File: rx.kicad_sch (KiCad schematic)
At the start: 49 parts, among them J5 SWH, J7 SMA, J9 SWH, T1 RF_BALUN, T1 RXIF_BALUN, U14 MAX2120, U16 DPDT

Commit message: Add footprints
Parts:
- C86, C89: footprint (none) -> Capacitor_SMD:C_0201_0603Metric
- FL2: footprint (none) -> mainboard:Filter_Pulse_LPF1005LL50R2400A_1.5x0.5mm
- J5, J9: footprint (none) -> mainboard:Murata_SWH_MM8930-26xx
- J7: footprint (none) -> mainboard:Linx_SMA_CONSMA003.062
- L6, L7: footprint (none) -> Inductor_SMD:L_0201_0603Metric
- R58, R59: footprint (none) -> Resistor_SMD:R_0201_0603Metric
- T1: footprint (none) -> RF_Converter:Balun_Johanson_0896BM15A0001
- T1: footprint (none) -> RF_Converter:Anaren_0805_2012Metric-6
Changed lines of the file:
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@@
       (effects (font (size 1.27 1.27)) (justify left))
     )
-    (property "Footprint" "" (at 110.1852 124.46 0)
+    (property "Footprint" "Capacitor_SMD:C_0201_0603Metric" (at 110.1852 124.46 0)
       (effects (font (size 1.27 1.27)) hide)
     )
@@
       (effects (font (size 1.27 1.27)))
     )
-    (property "Footprint" "" (at 124.1552 96.52 0)
+    (property "Footprint" "Capacitor_SMD:C_0201_0603Metric" (at 124.1552 96.52 0)
       (effects (font (size 1.27 1.27)) hide)
     )
@@
       (effects (font (size 1.27 1.27)))
     )
-    (property "Footprint" "" (at 179.07 44.45 0)
+    (property "Footprint" "mainboard:Filter_Pulse_LPF1005LL50R2400A_1.5x0.5mm" (at 179.07 44.45 0)
       (effects (font (size 1.27 1.27)) hide)
     )
@@
       (effects (font (size 1.27 1.27)))
     )
-    (property "Footprint" "" (at 121.412 91.44 90)
+    (property "Footprint" "Resistor_SMD:R_0201_0603Metric" (at 121.412 91.44 90)
       (effects (font (size 1.27 1.27)) hide)
     )
@@
       (effects (font (size 1.27 1.27)))
     )
-    (property "Footprint" "" (at 162.56 57.15 0)
+    (property "Footprint" "mainboard:Murata_SWH_MM8930-26xx" (at 162.56 57.15 0)
       (effects (font (size 1.27 1.27)) hide)
     )
@@
       (effects (font (size 1.27 1.27)))
     )
-    (property "Footprint" "" (at 232.41 101.6 0)
+    (property "Footprint" "RF_Converter:Balun_Johanson_0896BM15A0001" (at 232.41 101.6 0)
       (effects (font (size 1.27 1.27)) hide)
     )
@@
       (effects (font (size 1.27 1.27)))
     )
-    (property "Footprint" "" (at 231.14 67.31 0)
+    (property "Footprint" "mainboard:Murata_SWH_MM8930-26xx" (at 231.14 67.31 0)
       (effects (font (size 1.27 1.27)) hide)
     )
@@
       (effects (font (size 1.27 1.27)) (justify left))
     )
-    (property "Footprint" "" (at 185.42 90.17 0)
+    (property "Footprint" "Inductor_SMD:L_0201_0603Metric" (at 185.42 90.17 0)
       (effects (font (size 1.27 1.27)) hide)
     )
@@
       (effects (font (size 1.27 1.27)) (justify left))
     )
-    (property "Footprint" "" (at 224.79 92.71 0)
+    (property "Footprint" "Inductor_SMD:L_0201_0603Metric" (at 224.79 92.71 0)
       (effects (font (size 1.27 1.27)) hide)
     )
@@
       (effects (font (size 1.27 1.27)))
     )
-    (property "Footprint" "" (at 128.27 88.138 90)
+    (property "Footprint" "Resistor_SMD:R_0201_0603Metric" (at 128.27 88.138 90)
       (effects (font (size 1.27 1.27)) hide)
     )
@@
       (effects (font (size 1.27 1.27)))
     )
-    (property "Footprint" "" (at 176.53 99.06 0)
+    (property "Footprint" "RF_Converter:Anaren_0805_2012Metric-6" (at 176.53 99.06 0)
       (effects (font (size 1.27 1.27)) hide)
     )
@@
       (effects (font (size 1.27 1.27)) (justify left))
     )
-    (property "Footprint" "" (at 257.81 57.15 0)
-      (effects (font (size 1.27 1.27)) hide)
-    )
+    (property "Footprint" "mainboard:Linx_SMA_CONSMA003.062" (at 257.81 57.15 0)
+      (effects (font (size 1.27 1.27)) hide)
+    )

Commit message: Add more footprints
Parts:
- U16: footprint eval:QFN-12-1EP_2x2mm_P0.5mm_EP1x1mm -> mainboard:QFN-12-1EP_2x2mm_P0.5mm_EP1x1mm
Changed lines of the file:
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@@
       (effects (font (size 1.27 1.27)) (justify right))
     )
-    (property "Footprint" "eval:QFN-12-1EP_2x2mm_P0.5mm_EP1x1mm" (at 200.66 57.15 0)
+    (property "Footprint" "mainboard:QFN-12-1EP_2x2mm_P0.5mm_EP1x1mm" (at 200.66 57.15 0)
       (effects (font (size 1.27 1.27)) hide)
     )

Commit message: layout wip
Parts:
- added C159 (x2): 1uF, Capacitor_SMD:C_0201_0603Metric, symbol Device:C
- added J13: RFShield_Frame, RF_Shielding:Laird_Technologies_BMI-S-203-F_26.21x26.21mm, symbol Device:RFShield_OnePiece
- C159, C36: footprint Capacitor_SMD:C_0402_1005Metric -> Capacitor_SMD:C_0201_0603Metric; Manufacturer Samsung -> Murata; Part Number CL05A105KP5NNNC -> GRM033R61A105ME44D; Substitution any equivalent -> GRM033R61A105ME44*, GRM033R61C105ME15*, Samsung CL03A105MO3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
- C5: footprint Capacitor_SMD:C_0402_1005Metric -> Capacitor_SMD:C_0201_0603Metric; Manufacturer Samsung -> Murata; Part Number CL05B102KB5NNNC -> GRM033R71E102KA01D; Substitution any equivalent -> GRM033R71E102KA01*
- U16: footprint mainboard:QFN-12-1EP_2x2mm_P0.5mm_EP1x1mm -> mainboard:QFN-12-1EP_2x2mm_P0.5mm_EP1x1mm_ThermalVias
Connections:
- net 3V3RX: now also C159.1, C159.1
- net GND: now also C159.2, C159.2, J13.1 (Shield)
- net RX Mixer/MIX_IN+: now also L6.2, T1.4; no longer L6.1, T1.3
- net RX Mixer/MIX_IN-: now also L6.1, T1.3; no longer L6.2, T1.4

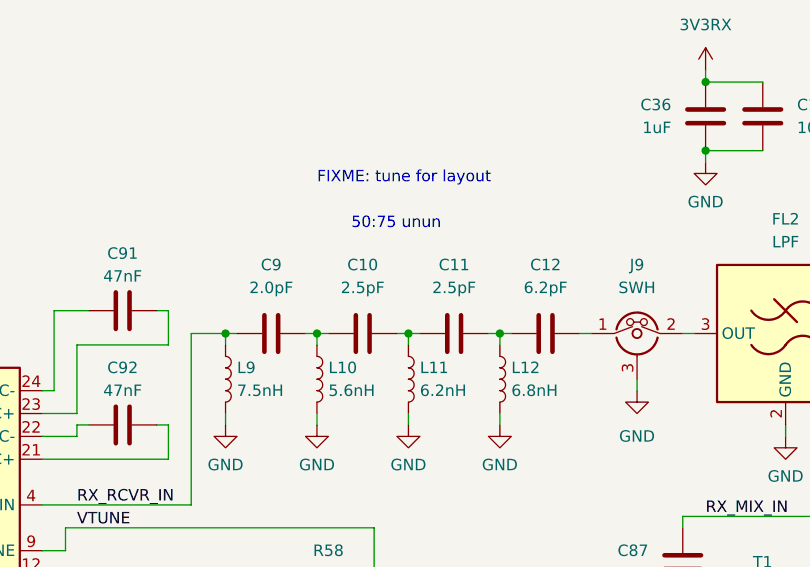
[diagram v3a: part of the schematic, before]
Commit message: tune unun for layout
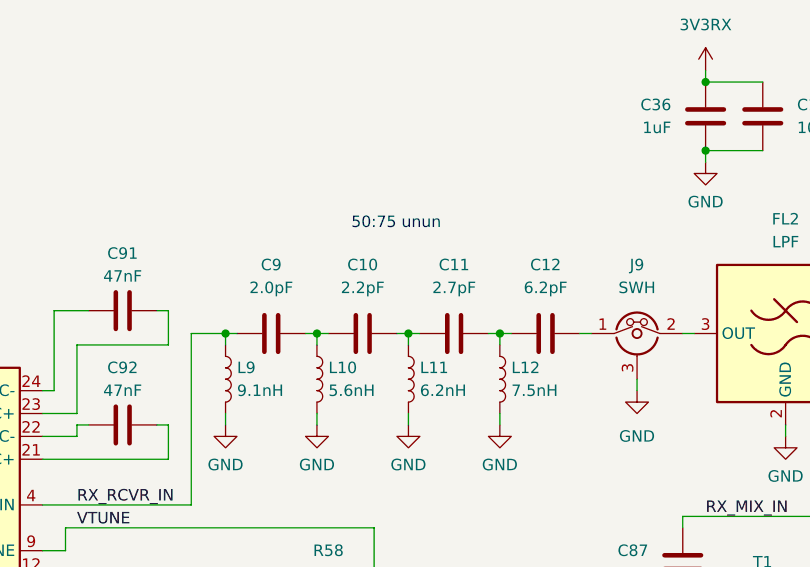
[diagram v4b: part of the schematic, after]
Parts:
- C10: value 2.5pF -> 2.2pF; Part Number GRM0335C1H2R5BA01D -> GRM0335C1H2R2BA01D; Substitution GRM0335C1H2R5BA01* -> GRM0335C1H2R2BA01*
- C11: value 2.5pF -> 2.7pF; Part Number GRM0335C1H2R5BA01D -> GRM0335C1H2R7BA01D; Substitution GRM0335C1H2R5BA01* -> GRM0335C1H2R7BA01*
- L12: value 6.8nH -> 7.5nH; Part Number LQP03HQ6N8H02D -> LQP03HQ7N5H02D
- L9: value 7.5nH -> 9.1nH; Part Number LQP03HQ7N5H02D -> LQP03HQ9N1H02D
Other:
- note removed: "FIXME: tune for layout"
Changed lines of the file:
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@@
-    (effects (font (size 1.27 1.27)) (justify left bottom))
-  )
-  (text "FIXME: tune for layout" (at 127 40.64 0)
     (effects (font (size 1.27 1.27)) (justify left bottom))
   )
@@
       (effects (font (size 1.27 1.27)))
     )
-    (property "Value" "2.5pF" (at 132.08 52.07 90)
+    (property "Value" "2.2pF" (at 132.08 52.07 90)
       (effects (font (size 1.27 1.27)))
     )
@@
       (effects (font (size 1.27 1.27)) hide)
     )
-    (property "Description" "CAP CER 2.5PF 50V C0G/NP0 0201" (at 132.08 57.15 0)
+    (property "Description" "CAP CER 2.2PF 50V C0G/NP0 0201" (at 132.08 57.15 0)
       (effects (font (size 1.27 1.27)) hide)
     )
@@
       (effects (font (size 1.27 1.27)) hide)
     )
-    (property "Part Number" "GRM0335C1H2R5BA01D" (at 132.08 57.15 0)
-      (effects (font (size 1.27 1.27)) hide)
-    )
-    (property "Substitution" "GRM0335C1H2R5BA01*" (at 132.08 57.15 0)
+    (property "Part Number" "GRM0335C1H2R2BA01D" (at 132.08 57.15 0)
+      (effects (font (size 1.27 1.27)) hide)
+    )
+    (property "Substitution" "GRM0335C1H2R2BA01*" (at 132.08 57.15 0)
       (effects (font (size 1.27 1.27)) hide)
     )
@@
       (effects (font (size 1.27 1.27)) (justify left))
     )
-    (property "Value" "7.5nH" (at 118.11 63.5 0)
+    (property "Value" "9.1nH" (at 118.11 63.5 0)
       (effects (font (size 1.27 1.27)) (justify left))
     )
@@
       (effects (font (size 1.27 1.27)) hide)
     )
-    (property "Description" "FIXED IND 7.5NH 400MA 300MOHM SM" (at 116.84 62.23 0)
+    (property "Description" "FIXED IND 9.1NH 300MA 400MOHM SM" (at 116.84 62.23 0)
       (effects (font (size 1.27 1.27)) hide)
     )
@@
       (effects (font (size 1.27 1.27)) hide)
     )
-    (property "Part Number" "LQP03HQ7N5H02D" (at 116.84 62.23 0)
+    (property "Part Number" "LQP03HQ9N1H02D" (at 116.84 62.23 0)
       (effects (font (size 1.27 1.27)) hide)
     )
@@
       (effects (font (size 1.27 1.27)) (justify left))
     )
-    (property "Value" "6.8nH" (at 148.59 63.5 0)
+    (property "Value" "7.5nH" (at 148.59 63.5 0)
       (effects (font (size 1.27 1.27)) (justify left))
     )
@@
       (effects (font (size 1.27 1.27)) hide)
     )
-    (property "Description" "FIXED IND 6.8NH 400MA 300MOHM SM" (at 147.32 62.23 0)
+    (property "Description" "FIXED IND 7.5NH 400MA 300MOHM SM" (at 147.32 62.23 0)
       (effects (font (size 1.27 1.27)) hide)
     )
@@
       (effects (font (size 1.27 1.27)) hide)
     )
-    (property "Part Number" "LQP03HQ6N8H02D" (at 147.32 62.23 0)
+    (property "Part Number" "LQP03HQ7N5H02D" (at 147.32 62.23 0)
       (effects (font (size 1.27 1.27)) hide)
     )
@@
       (effects (font (size 1.27 1.27)))
     )
-    (property "Value" "2.5pF" (at 142.24 52.07 90)
+    (property "Value" "2.7pF" (at 142.24 52.07 90)
       (effects (font (size 1.27 1.27)))
     )
@@
       (effects (font (size 1.27 1.27)) hide)
     )
-    (property "Description" "CAP CER 2.5PF 50V C0G/NP0 0201" (at 142.24 57.15 0)
+    (property "Description" "CAP CER 2.7PF 50V C0G/NP0 0201" (at 142.24 57.15 0)
       (effects (font (size 1.27 1.27)) hide)
     )
@@
       (effects (font (size 1.27 1.27)) hide)
     )
-    (property "Part Number" "GRM0335C1H2R5BA01D" (at 142.24 57.15 0)
-      (effects (font (size 1.27 1.27)) hide)
-    )
-    (property "Substitution" "GRM0335C1H2R5BA01*" (at 142.24 57.15 0)
-      (effects (font (size 1.27 1.27)) hide)
-    )
+    (property "Part Number" "GRM0335C1H2R7BA01D" (at 142.24 57.15 0)
+      (effects (font (size 1.27 1.27)) hide)
+    )
+    (property "Substitution" "GRM0335C1H2R7BA01*" (at 142.24 57.15 0)
+      (effects (font (size 1.27 1.27)) hide)
+    )

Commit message: passive component selections
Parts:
- C89: Manufacturer (none) -> Murata; Part Number (none) -> GRM033R61A333KE84D; Substitution (none) -> GRM033R61A333KE84*
- C91, C92: Manufacturer (none) -> Murata; Part Number (none) -> GRM033R60J473KE19D; Substitution (none) -> GRM033R60J473KE19*
- R58: Manufacturer (none) -> Yageo; Part Number (none) -> RC0201JR-07820RL; Substitution (none) -> any equivalent
- R59: Manufacturer (none) -> Yageo; Part Number (none) -> RC0201JR-07390RL; Substitution (none) -> any equivalent
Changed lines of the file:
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@@
+      (effects (font (size 1.27 1.27)) hide)
+    )
+    (property "Description" "CAP CER 0.033UF 10V X5R 0201" (at 123.19 100.33 0)
+      (effects (font (size 1.27 1.27)) hide)
+    )
+    (property "Manufacturer" "Murata" (at 123.19 100.33 0)
+      (effects (font (size 1.27 1.27)) hide)
+    )
+    (property "Part Number" "GRM033R61A333KE84D" (at 123.19 100.33 0)
+      (effects (font (size 1.27 1.27)) hide)
+    )
+    (property "Substitution" "GRM033R61A333KE84*" (at 123.19 100.33 0)
       (effects (font (size 1.27 1.27)) hide)
     )
@@
       (effects (font (size 1.27 1.27)) hide)
     )
+    (property "Description" "RES 390 OHM 5% 1/20W 0201" (at 123.19 91.44 0)
+      (effects (font (size 1.27 1.27)) hide)
+    )
+    (property "Manufacturer" "Yageo" (at 123.19 91.44 0)
+      (effects (font (size 1.27 1.27)) hide)
+    )
+    (property "Part Number" "RC0201JR-07390RL" (at 123.19 91.44 0)
+      (effects (font (size 1.27 1.27)) hide)
+    )
+    (property "Substitution" "any equivalent" (at 123.19 91.44 0)
+      (effects (font (size 1.27 1.27)) hide)
+    )
     (pin "1")
     (pin "2")
@@
       (effects (font (size 1.27 1.27)) hide)
     )
+    (property "Description" "CAP CER 0.047UF 6.3V X5R 0201" (at 105.41 67.31 0)
+      (effects (font (size 1.27 1.27)) hide)
+    )
+    (property "Manufacturer" "Murata" (at 105.41 67.31 0)
+      (effects (font (size 1.27 1.27)) hide)
+    )
+    (property "Part Number" "GRM033R60J473KE19D" (at 105.41 67.31 0)
+      (effects (font (size 1.27 1.27)) hide)
+    )
+    (property "Substitution" "GRM033R60J473KE19*" (at 105.41 67.31 0)
+      (effects (font (size 1.27 1.27)) hide)
+    )
     (pin "1")
     (pin "2")
@@
     )
     (property "Datasheet" "~" (at 105.41 54.61 0)
+      (effects (font (size 1.27 1.27)) hide)
+    )
+    (property "Description" "CAP CER 0.047UF 6.3V X5R 0201" (at 105.41 54.61 0)
+      (effects (font (size 1.27 1.27)) hide)
+    )
+    (property "Manufacturer" "Murata" (at 105.41 54.61 0)
+      (effects (font (size 1.27 1.27)) hide)
+    )
+    (property "Part Number" "GRM033R60J473KE19D" (at 105.41 54.61 0)
+      (effects (font (size 1.27 1.27)) hide)
+    )
+    (property "Substitution" "GRM033R60J473KE19*" (at 105.41 54.61 0)
       (effects (font (size 1.27 1.27)) hide)
     )
@@
       (effects (font (size 1.27 1.27)) hide)
     )
+    (property "Description" "RES 820 OHM 5% 1/20W 0201" (at 128.27 86.36 0)
+      (effects (font (size 1.27 1.27)) hide)
+    )
+    (property "Manufacturer" "Yageo" (at 128.27 86.36 0)
+      (effects (font (size 1.27 1.27)) hide)
+    )
+    (property "Part Number" "RC0201JR-07820RL" (at 128.27 86.36 0)
+      (effects (font (size 1.27 1.27)) hide)
+    )
+    (property "Substitution" "any equivalent" (at 128.27 86.36 0)
+      (effects (font (size 1.27 1.27)) hide)
+    )
